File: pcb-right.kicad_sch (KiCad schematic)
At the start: 38 parts, among them SW19 GENERIC_ELECTROMECHANICAL_PUS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, SW20 GENERIC_ELECTROMECHANICAL_PUS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, SW21 GENERIC_ELECTROMECHANICAL_PUS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, SW22 GENERIC_ELECTROMECHANICAL_PUS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, SW23 GENERIC_ELECTROMECHANICAL_PUS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, SW24 GENERIC_ELECTROMECHANICAL_PUS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, SW25 GENERIC_ELECTROMECHANICAL_PUS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, SW26 GENERIC_ELECTROMECHANICAL_PUS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, SW27 GENERIC_ELECTROMECHANICAL_PUS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, SW28 GENERIC_ELECTROMECHANICAL_PUS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, SW29 GENERIC_ELECTROMECHANICAL_PUS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, SW30 GENERIC_ELECTROMECHANICAL_PUS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, SW31 GENERIC_ELECTROMECHANICAL_PUS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, SW32 GENERIC_ELECTROMECHANICAL_PUS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, SW33 GENERIC_ELECTROMECHANICAL_PUS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, SW34 GENERIC_ELECTROMECHANICAL_PUS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, SW35 GENERIC_ELECTROMECHANICAL_PUS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, SW36 GENERIC_ELECTROMECHANICAL_PUS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, U2 XIAO-RP2040-DIP

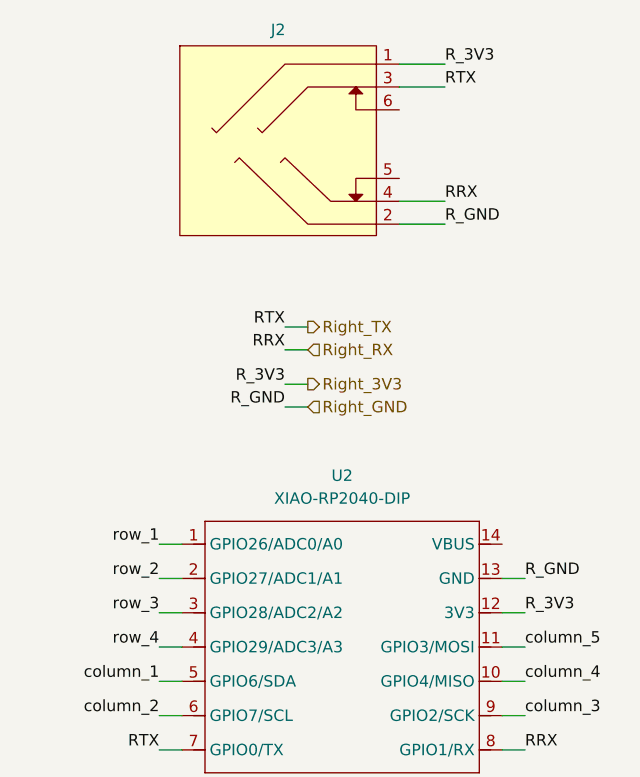
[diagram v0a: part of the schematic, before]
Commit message: Rev 1.1, fix diode footprints, add plate and base generation jobs, add mouse bites and some extra solder jumpers
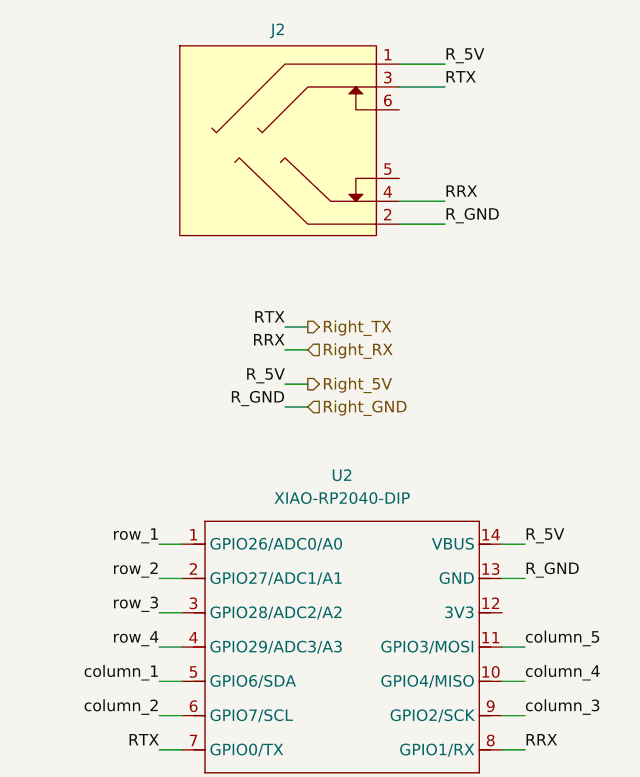
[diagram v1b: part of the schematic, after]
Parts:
- SW19, SW20, SW21, SW22, SW23, SW24, SW25, SW26, SW27, SW28, SW29, SW30, SW31, SW32, SW33, SW34, SW35, SW36: footprint benri-projects:GatereonHotswap -> benri-projects:GATEREON_KS-2P02B01-01-a_R
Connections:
- net Right_5V: now reaches U2.14 (VBUS)
- net Right_5V: now also J2.1
- net Right_3V3: no longer names the net of U2.12 (3V3)
- net Right_3V3: no longer J2.1
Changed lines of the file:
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@@
 	(wire
 		(pts
-			(xy 243.84 111.76) (xy 246.38 111.76)
-		)
-		(stroke
-			(width 0)
-			(type default)
-		)
-	)
-	(wire
-		(pts
 			(xy 146.05 59.69) (xy 146.05 62.23)
 		)
@@
 	(wire
 		(pts
+			(xy 243.84 104.14) (xy 246.38 104.14)
+		)
+		(stroke
+			(width 0)
+			(type default)
+		)
+	)
+	(wire
+		(pts
 			(xy 76.2 116.84) (xy 77.47 116.84)
 		)
@@
 		)
 	)
-	(label "R_3V3"
-		(at 246.38 111.76 0)
+	(label "R_5V"
+		(at 246.38 104.14 0)
 		(effects
 			(font
@@
 		)
 	)
-	(label "R_3V3"
+	(label "R_5V"
 		(at 237.49 50.8 0)
 		(effects
@@
 		)
 	)
-	(label "R_3V3"
+	(label "R_5V"
 		(at 219.71 86.36 180)
 		(effects
@@
 		)
 	)
-	(hierarchical_label "Right_3V3"
+	(hierarchical_label "Right_5V"
 		(shape output)
 		(at 222.25 86.36 0)
@@
 			)
 		)
-		(property "Footprint" "benri-projects:GatereonHotswap"
+		(property "Footprint" "benri-projects:GATEREON_KS-2P02B01-01-a_R"
 			(at 138.43 73.66 0)
 			(effects
@@
 			)
 		)
-		(property "Footprint" "benri-projects:GatereonHotswap"
+		(property "Footprint" "benri-projects:GATEREON_KS-2P02B01-01-a_R"
 			(at 63.5 111.76 0)
 			(effects
@@
 			)
 		)
-		(property "Footprint" "benri-projects:GatereonHotswap"
+		(property "Footprint" "benri-projects:GATEREON_KS-2P02B01-01-a_R"
 			(at 63.5 92.71 0)
 			(effects
@@
 			)
 		)
-		(property "Footprint" "benri-projects:GatereonHotswap"
+		(property "Footprint" "benri-projects:GATEREON_KS-2P02B01-01-a_R"
 			(at 156.21 73.66 0)
 			(effects
@@
 			)
 		)
-		(property "Footprint" "benri-projects:GatereonHotswap"
+		(property "Footprint" "benri-projects:GATEREON_KS-2P02B01-01-a_R"
 			(at 101.6 92.71 0)
 			(effects
@@
 			)
 		)
-		(property "Footprint" "benri-projects:GatereonHotswap"
+		(property "Footprint" "benri-projects:GATEREON_KS-2P02B01-01-a_R"
 			(at 156.21 54.61 0)
 			(effects
@@
 			)
 		)
-		(property "Footprint" "benri-projects:GatereonHotswap"
+		(property "Footprint" "benri-projects:GATEREON_KS-2P02B01-01-a_R"
 			(at 82.55 73.66 0)
 			(effects
@@
 			)
 		)
-		(property "Footprint" "benri-projects:GatereonHotswap"
+		(property "Footprint" "benri-projects:GATEREON_KS-2P02B01-01-a_R"
 			(at 119.38 54.61 0)
 			(effects
@@
 			)
 		)
-		(property "Footprint" "benri-projects:GatereonHotswap"
+		(property "Footprint" "benri-projects:GATEREON_KS-2P02B01-01-a_R"
 			(at 63.5 54.61 0)
 			(effects
@@
 			)
 		)
-		(property "Footprint" "benri-projects:GatereonHotswap"
+		(property "Footprint" "benri-projects:GATEREON_KS-2P02B01-01-a_R"
 			(at 119.38 92.71 0)
 			(effects
@@
 			)
 		)
-		(property "Footprint" "benri-projects:GatereonHotswap"
+		(property "Footprint" "benri-projects:GATEREON_KS-2P02B01-01-a_R"
 			(at 82.55 92.71 0)
 			(effects
@@
 			)
 		)
-		(property "Footprint" "benri-projects:GatereonHotswap"
+		(property "Footprint" "benri-projects:GATEREON_KS-2P02B01-01-a_R"
 			(at 138.43 54.61 0)
 			(effects
@@
 			)
 		)
-		(property "Footprint" "benri-projects:GatereonHotswap"
+		(property "Footprint" "benri-projects:GATEREON_KS-2P02B01-01-a_R"
 			(at 101.6 54.61 0)
 			(effects
@@
 			)
 		)
-		(property "Footprint" "benri-projects:GatereonHotswap"
+		(property "Footprint" "benri-projects:GATEREON_KS-2P02B01-01-a_R"
 			(at 82.55 54.61 0)
 			(effects
@@
 			)
 		)
-		(property "Footprint" "benri-projects:GatereonHotswap"
+		(property "Footprint" "benri-projects:GATEREON_KS-2P02B01-01-a_R"
 			(at 119.38 73.66 0)
 			(effects
@@
 			)
 		)
-		(property "Footprint" "benri-projects:GatereonHotswap"
+		(property "Footprint" "benri-projects:GATEREON_KS-2P02B01-01-a_R"
 			(at 101.6 73.66 0)
 			(effects
@@
 			)
 		)
-		(property "Footprint" "benri-projects:GatereonHotswap"
+		(property "Footprint" "benri-projects:GATEREON_KS-2P02B01-01-a_R"
 			(at 63.5 73.66 0)
 			(effects
@@
 			)
 		)
-		(property "Footprint" "benri-projects:GatereonHotswap"
+		(property "Footprint" "benri-projects:GATEREON_KS-2P02B01-01-a_R"
 			(at 82.55 111.76 0)
 			(effects

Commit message: Touchups and name: Logos
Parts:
- U2: footprint Seeed Studio XIAO Series Library:XIAO-RP2040-DIP -> benri-projects:SEEED_XIAO-RP2040_T-DIP
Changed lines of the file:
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@@
 			)
 		)
-		(property "Footprint" "Seeed Studio XIAO Series Library:XIAO-RP2040-DIP"
+		(property "Footprint" "benri-projects:SEEED_XIAO-RP2040_T-DIP"
 			(at 226.568 131.318 0)
 			(effects

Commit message: Latest release
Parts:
- removed J2: ~, benri-projects:TENSILITY_54-00176_R, symbol benri-projects:CONNECTOR_TENSILITY_54-00176
- added J2: (no value), symbol benri-projects:CONNECTOR_JST_SM04B-SRSS-TB
- U2: footprint benri-projects:SEEED_XIAO-RP2040_T-DIP -> Module:MOUDLE14P-XIAO-DIP-SMD
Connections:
- net Right_5V: now also J2.1
- net Right_GND: now also J2.4
- net Right_RX: now also J2.3
- net Right_TX: now also J2.2

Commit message: Through hole layout
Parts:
- removed J2: (no value), symbol benri-projects:CONNECTOR_JST_SM04B-SRSS-TB
- D19, D20, D21, D22, D23, D24, D25, D26, D27, D28, D29, D30, D31, D32, D33, D34, D35, D36: footprint benri-projects:DIODES_SOD232_R -> benri-projects:GENERIC_DO-35_A
- U2: footprint Module:MOUDLE14P-XIAO-DIP-SMD -> benri-projects:SEEED_XIAO-RP2040_T-DIP
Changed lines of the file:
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@@
 	(wire
 		(pts
-			(xy 223.52 64.77) (xy 228.6 64.77)
-		)
-		(stroke
-			(width 0)
-			(type default)
-		)
-	)
-	(wire
-		(pts
 			(xy 163.83 106.68) (xy 127 106.68)
 		)
@@
 	(wire
 		(pts
-			(xy 57.15 59.69) (xy 58.42 59.69)
+			(xy 163.83 86.36) (xy 163.83 106.68)
 		)
 		(stroke
@@
 	(wire
 		(pts
-			(xy 57.15 116.84) (xy 58.42 116.84)
+			(xy 57.15 59.69) (xy 58.42 59.69)
 		)
 		(stroke
@@
 	(wire
 		(pts
-			(xy 57.15 97.79) (xy 58.42 97.79)
+			(xy 57.15 116.84) (xy 58.42 116.84)
 		)
 		(stroke
@@
 	(wire
 		(pts
-			(xy 146.05 67.31) (xy 146.05 68.58)
+			(xy 57.15 97.79) (xy 58.42 97.79)
 		)
 		(stroke
@@
 	(wire
 		(pts
-			(xy 243.84 107.95) (xy 246.38 107.95)
+			(xy 146.05 67.31) (xy 146.05 68.58)
 		)
 		(stroke
@@
 	(wire
 		(pts
-			(xy 163.83 86.36) (xy 163.83 106.68)
+			(xy 243.84 107.95) (xy 246.38 107.95)
 		)
 		(stroke
@@
 	(wire
 		(pts
-			(xy 223.52 72.39) (xy 228.6 72.39)
-		)
-		(stroke
-			(width 0)
-			(type default)
-		)
-	)
-	(wire
-		(pts
 			(xy 109.22 106.68) (xy 90.17 106.68)
 		)
@@
 	(wire
 		(pts
-			(xy 223.52 69.85) (xy 228.6 69.85)
-		)
-		(stroke
-			(width 0)
-			(type default)
-		)
-	)
-	(wire
-		(pts
 			(xy 109.22 97.79) (xy 109.22 100.33)
 		)
@@
 	(wire
 		(pts
-			(xy 223.52 67.31) (xy 228.6 67.31)
-		)
-		(stroke
-			(width 0)
-			(type default)
-		)
-	)
-	(wire
-		(pts
 			(xy 132.08 49.53) (xy 132.08 52.07)
 		)
@@
 		)
 	)
-	(label "RRX"
-		(at 228.6 69.85 0)
-		(effects
-			(font
-				(size 1.27 1.27)
-			)
-			(justify left bottom)
-		)
-	)
 	(label "row_4"
 		(at 205.74 115.57 180)
@@
 		)
 	)
-	(label "R_GND"
-		(at 228.6 72.39 0)
-		(effects
-			(font
-				(size 1.27 1.27)
-			)
-			(justify left bottom)
-		)
-	)
 	(label "column_4"
 		(at 246.38 119.38 0)
@@
 		)
 	)
-	(label "RTX"
-		(at 228.6 67.31 0)
-		(effects
-			(font
-				(size 1.27 1.27)
-			)
-			(justify left bottom)
-		)
-	)
-	(label "R_5V"
-		(at 228.6 64.77 0)
-		(effects
-			(font
-				(size 1.27 1.27)
-			)
-			(justify left bottom)
-		)
-	)
 	(label "R_5V"
 		(at 219.71 86.36 180)
@@
 			)
 		)
-		(property "Footprint" "benri-projects:DIODES_SOD232_R"
+		(property "Footprint" "benri-projects:GENERIC_DO-35_A"
 			(at 116.84 83.82 0)
 			(hide yes)
@@
 			)
 		)
-		(property "Footprint" "benri-projects:DIODES_SOD232_R"
+		(property "Footprint" "benri-projects:GENERIC_DO-35_A"
 			(at 153.67 64.77 0)
 			(hide yes)
@@
 			)
 		)
-		(property "Footprint" "benri-projects:DIODES_SOD232_R"
+		(property "Footprint" "benri-projects:GENERIC_DO-35_A"
 			(at 135.89 64.77 0)
 			(hide yes)
@@
 			)
 		)
-		(property "Footprint" "benri-projects:DIODES_SOD232_R"
+		(property "Footprint" "benri-projects:GENERIC_DO-35_A"
 			(at 60.96 64.77 0)
 			(hide yes)
@@
 			)
 		)
-		(property "Footprint" "benri-projects:DIODES_SOD232_R"
+		(property "Footprint" "benri-projects:GENERIC_DO-35_A"
 			(at 80.01 121.92 0)
 			(hide yes)
@@
 			)
 		)
-		(property "Footprint" "benri-projects:DIODES_SOD232_R"
+		(property "Footprint" "benri-projects:GENERIC_DO-35_A"
 			(at 80.01 102.87 0)
 			(hide yes)
@@
 			)
 		)
-		(property "Footprint" "benri-projects:DIODES_SOD232_R"
+		(property "Footprint" "benri-projects:GENERIC_DO-35_A"
 			(at 80.01 64.77 0)
 			(hide yes)
@@
 			)
 		)
-		(property "Footprint" "benri-projects:DIODES_SOD232_R"
+		(property "Footprint" "benri-projects:GENERIC_DO-35_A"
 			(at 99.06 64.77 0)
 			(hide yes)
@@
 	)
 	(symbol
-		(lib_id "benri-projects:CONNECTOR_JST_SM04B-SRSS-TB")
-		(at 218.44 68.58 0)
-		(mirror y)
-		(unit 1)
-		(body_style 1)
-		(exclude_from_sim no)
-		(in_bom yes)
-		(on_board yes)
-		(in_pos_files yes)
-		(dnp no)
-		(fields_autoplaced yes)
-		(property "Reference" "J2"
-			(at 218.44 60.96 0)
-			(show_name no)
-			(do_not_autoplace no)
-			(effects
-				(font
-					(size 1.27 1.27)
-				)
-			)
-		)
-		(property "Value" ""
-			(at 218.44 68.58 0)
-			(show_name no)
-			(do_not_autoplace no)
-			(effects
-				(font
-					(size 1.27 1.27)
-				)
-			)
-		)
-		(property "Footprint" ""
-			(at 218.44 68.58 0)
-			(hide yes)
-			(show_name no)
-			(do_not_autoplace no)
-			(effects
-				(font
-					(size 1.27 1.27)
-				)
-			)
-		)
-		(property "Datasheet" ""
-			(at 218.44 68.58 0)
-			(hide yes)
-			(show_name no)
-			(do_not_autoplace no)
-			(effects
-				(font
-					(size 1.27 1.27)
-				)
-			)
-		)
-		(property "Description" ""
-			(at 218.44 68.58 0)
-			(hide yes)
-			(show_name no)
-			(do_not_autoplace no)
-			(effects
-				(font
-					(size 1.27 1.27)
-				)
-			)
-		)
-		(pin "1"
-		)
-		(pin "2"
-		)
-		(pin "3"
-		)
-		(pin "4"
-		)
-		(instances
-			(project "keyboard-split-splay-5x3+2-pinky-cluster"
-				(path "/81ff113e-ae40-4f69-bd5b-ccd6a1ee23eb/1e51f56e-c3ed-4ee6-89f9-75995dd4f842"
-					(reference "J2")
-					(unit 1)
-				)
-			)
-		)
-	)
-	(symbol
 		(lib_id "benri-projects:GENERIC_ELECTROMECHANICAL_PUSHBUTTON")
 		(at 119.38 97.79 0)
@@
 			)
 		)
-		(property "Footprint" "benri-projects:DIODES_SOD232_R"
+		(property "Footprint" "benri-projects:GENERIC_DO-35_A"
 			(at 99.06 83.82 0)
 			(hide yes)
@@
 			)
 		)
-		(property "Footprint" "benri-projects:DIODES_SOD232_R"
+		(property "Footprint" "benri-projects:GENERIC_DO-35_A"
 			(at 60.96 102.87 0)
 			(hide yes)
@@
 			)
 		)
-		(property "Footprint" "benri-projects:DIODES_SOD232_R"
+		(property "Footprint" "benri-projects:GENERIC_DO-35_A"
 			(at 80.01 83.82 0)
 			(hide yes)
@@
 			)
 		)
-		(property "Footprint" "Module:MOUDLE14P-XIAO-DIP-SMD"
+		(property "Footprint" "benri-projects:SEEED_XIAO-RP2040_T-DIP"
 			(at 226.568 131.318 0)
 			(hide yes)
@@
 			)
 		)
-		(property "Footprint" "benri-projects:DIODES_SOD232_R"
+		(property "Footprint" "benri-projects:GENERIC_DO-35_A"
 			(at 153.67 83.82 0)
 			(hide yes)
@@
 			)
 		)
-		(property "Footprint" "benri-projects:DIODES_SOD232_R"
+		(property "Footprint" "benri-projects:GENERIC_DO-35_A"
 			(at 116.84 102.87 0)
 			(hide yes)
@@
 			)
 		)
-		(property "Footprint" "benri-projects:DIODES_SOD232_R"
+		(property "Footprint" "benri-projects:GENERIC_DO-35_A"
 			(at 99.06 102.87 0)
 			(hide yes)
@@
 			)
 		)
-		(property "Footprint" "benri-projects:DIODES_SOD232_R"
+		(property "Footprint" "benri-projects:GENERIC_DO-35_A"
 			(at 135.89 83.82 0)
 			(hide yes)
@@
 			)
 		)
-		(property "Footprint" "benri-projects:DIODES_SOD232_R"
+		(property "Footprint" "benri-projects:GENERIC_DO-35_A"
 			(at 116.84 64.77 0)
 			(hide yes)
@@
 			)
 		)
-		(property "Footprint" "benri-projects:DIODES_SOD232_R"
+		(property "Footprint" "benri-projects:GENERIC_DO-35_A"
 			(at 60.96 83.82 0)
 			(hide yes)
@@
 			)
 		)
-		(property "Footprint" "benri-projects:DIODES_SOD232_R"
+		(property "Footprint" "benri-projects:GENERIC_DO-35_A"
 			(at 60.96 121.92 0)
 			(hide yes)
